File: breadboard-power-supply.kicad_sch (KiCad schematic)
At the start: 0 parts

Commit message: most of sch done
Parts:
- added C1, C4: 100nF, symbol DSE-Passives:C
- added C2, C6: 1uF, symbol DSE-Passives:C
- added C3, C5: 10uF, symbol DSE-Passives:C
- added D1, D2, D3, D4: ES1B-13-F, symbol DSE-Passives:D
- added J1, J2: PJ-002A, symbol Connector:Barrel_Jack_Switch
- added J3, J4, J5, J6: 61300211121, symbol Connector:Conn_01x02_Pin
- added R1, R4: 240R, symbol DSE-Passives:R
- added R2, R3: 390R, symbol DSE-Passives:R
- added R2, R5: 715R, symbol DSE-Passives:R
- added SW1, SW2: SW_SP3T, symbol Switch:SW_SP3T
- added SW3, SW4: 500SSP3S1M6QEA, symbol Switch:SW_SPDT
- added SW5: SW_DP3T, symbol Switch:SW_DP3T
- added U1, U2: LM317M, symbol lib_sch:LM317M
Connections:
- new net: R3.1, SW2.4
- new net: J2.1, SW4.2 (B)
- new net: R2.1, SW1.4
- new net: R2.1, SW1.2
- new net: J1.1, SW3.2 (B)
- new net: R5.1, SW2.2
- new net ADJ1: C3.1, C5.1, D2.1, D4.1, R1.2, R4.2, SW1.3, SW5.3, U1.1 (Adj), U2.1 (Adj)
- new net ADJ2: SW2.3
- new net GND: C1.2, C2.2, C3.2, C4.2, C5.2, C6.2, J1.2, J1.3, J2.2, J2.3, J3.2 (Pin_2), J5.2 (Pin_2), R2.2, R2.2, R3.2, R5.2
- new net VCC1: C2.1, D1.1, D2.2, J3.1 (Pin_1), R1.1, SW5.1, SW5.2, SW5.8, U1.2 (OUT), U1.4 (OUT)
- new net VCC2: C6.1, D3.1, D4.2, J5.1 (Pin_1), R4.1, U2.2 (OUT), U2.4 (OUT)
- new net VIN1: C1.1, D1.2, SW1.1, SW3.1 (A), SW5.7, U1.3 (IN)
- new net VIN2: C4.1, D3.2, SW2.1, SW4.1 (A), U2.3 (IN)
- no-connect marks 0 -> 9
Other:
- note added: "ADD INDICATOR LED"
- note added: "Vo=3V3"
- note added: "Vo=5V"

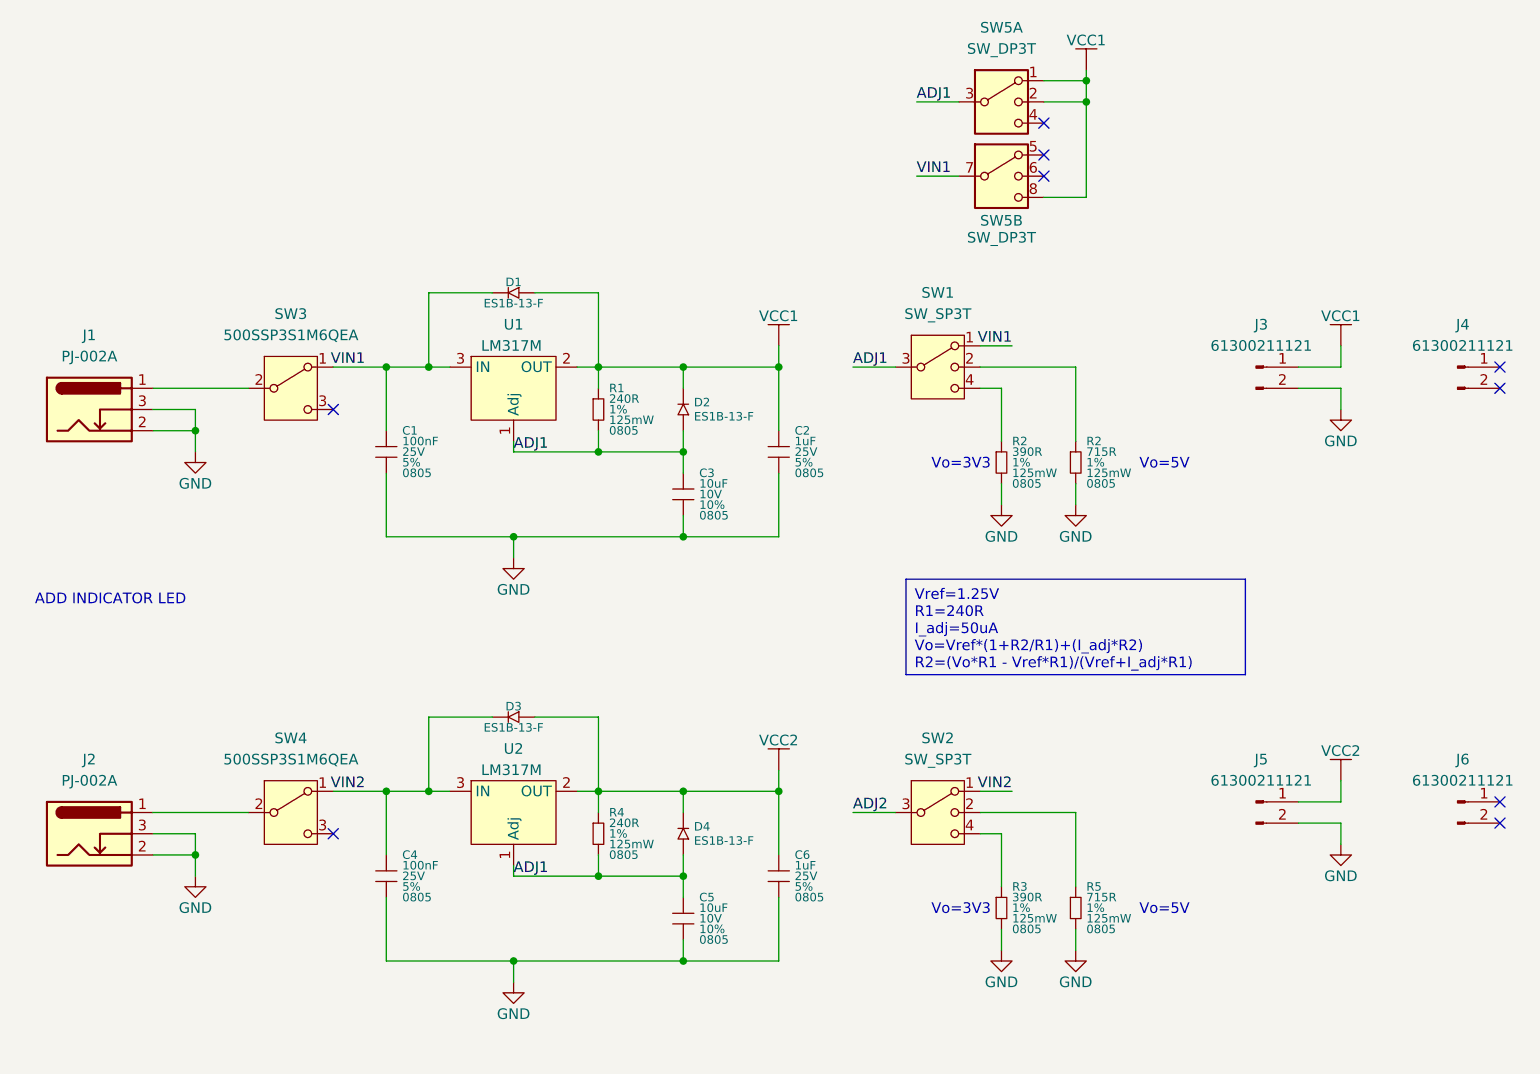
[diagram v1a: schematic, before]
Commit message: fixed switches in schematic
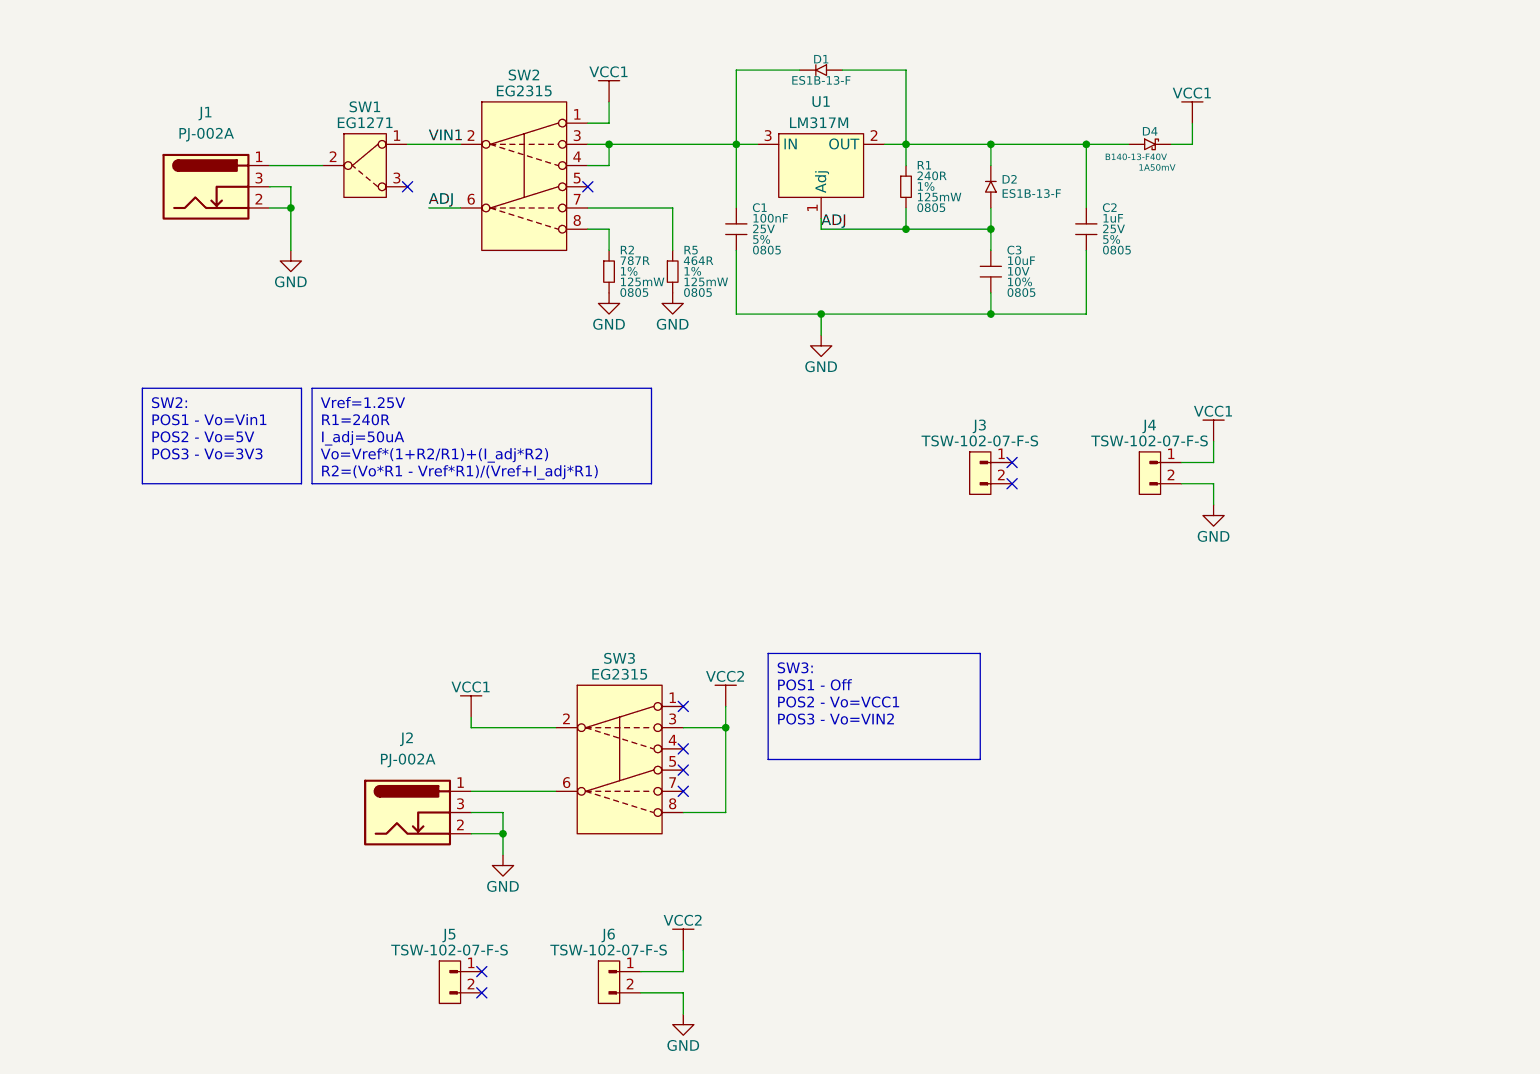
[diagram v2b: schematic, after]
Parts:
- removed C4: 100nF, symbol DSE-Passives:C
- removed C5: 10uF, symbol DSE-Passives:C
- removed C6: 1uF, symbol DSE-Passives:C
- removed D3, D4: ES1B-13-F, symbol DSE-Passives:D
- removed J2: PJ-002A, symbol Connector:Barrel_Jack_Switch
- removed J3, J4, J5, J6: 61300211121, symbol Connector:Conn_01x02_Pin
- removed R2, R3: 390R, symbol DSE-Passives:R
- removed R2, R5: 715R, symbol DSE-Passives:R
- removed R4: 240R, symbol DSE-Passives:R
- removed SW1, SW2: SW_SP3T, symbol Switch:SW_SP3T
- removed SW3, SW4: 500SSP3S1M6QEA, symbol Switch:SW_SPDT
- removed SW5: SW_DP3T, symbol Switch:SW_DP3T
- removed U2: LM317M, symbol lib_sch:LM317M
- added D4: B140-13-F, lib_fp:SMA, symbol lib_sch:D_Schottky_horizontal
- added J2: PJ-002A, lib_fp:PJ-002A, symbol lib_sch:Barrel_Jack_Switch
- added J3, J4, J5, J6: TSW-102-07-F-S, lib_fp:conn_01x02_254, symbol lib_sch:conn_01x02
- added R2: 787R, lib_fp:RESC200X125X60L35_35N, symbol lib_sch:R
- added R5: 464R, lib_fp:RESC200X125X60L35_35N, symbol lib_sch:R
- added SW1: EG1271, lib_fp:EG-1271, symbol lib_sch:EG-1271
- added SW2, SW3: EG2315, lib_fp:EG-2315, symbol lib_sch:DP3T
- C1, C2, C3: footprint (none) -> lib_fp:CAPC200X125X88L50N; symbol DSE-Passives:C -> lib_sch:C
- D1, D2: footprint (none) -> lib_fp:SMA; symbol DSE-Passives:D -> lib_sch:D
- J1: footprint (none) -> lib_fp:PJ-002A; symbol Connector:Barrel_Jack_Switch -> lib_sch:Barrel_Jack_Switch
- R1: footprint (none) -> lib_fp:RESC200X125X60L35_35N; symbol DSE-Passives:R -> lib_sch:R
- U1: footprint (none) -> lib_fp:SOT223-4
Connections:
- net GND: now also J2.2, J2.3, J4.2, J6.2, R2.2, R5.2
- net VCC1: now also D4.2, J4.1, SW2.1, SW3.2; no longer C2.1, D1.1, D2.2, R1.1, U1.2 (OUT), U1.4 (OUT)
- net VCC2: now also J6.1, SW3.3, SW3.8
- net VIN1: now also SW1.1, SW1.4, SW2.2; no longer C1.1, D1.2, U1.3 (IN)
- net at J1.1: now also SW1.2, SW1.5
- net ADJ1 renamed ADJ
- net ADJ: now also SW2.6
- new net: C2.1, D1.1, D2.2, D4.1, R1.1, U1.2 (OUT), U1.4 (OUT)
- new net: C1.1, D1.2, SW2.3, SW2.4, U1.3 (IN)
- new net: R5.1, SW2.7
- new net: R2.1, SW2.8
- new net: J2.1, SW3.6
- new net: SW1.3, SW1.6
- no-connect marks 9 -> 10
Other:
- note removed: "ADD INDICATOR LED"
- note removed: "Vo=3V3"
- note removed: "Vo=5V"
- moved on the sheet: C1, C2, C3, D1, D2, J1, R1, U1

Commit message: cleaned up files and scrubbed meta data
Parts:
- renumbered D4 to D3, R5 to R3
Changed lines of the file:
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@@
 		(dnp no)
 		(fields_autoplaced yes)
-		(property "Reference" "R5"
+		(property "Reference" "R3"
 			(at 134.62 85.09 0)
 			(do_not_autoplace yes)
@@
 			(project "breadboard-power-supply"
 				(path "/b84480f7-2a4a-488c-b5cb-7253df0ad470"
-					(reference "R5")
+					(reference "R3")
 					(unit 1)
 				)
@@
 		(dnp no)
 		(fields_autoplaced yes)
-		(property "Reference" "D4"
+		(property "Reference" "D3"
 			(at 190.5 70.866 0)
 			(do_not_autoplace yes)
@@
 			(project ""
 				(path "/b84480f7-2a4a-488c-b5cb-7253df0ad470"
-					(reference "D4")
+					(reference "D3")
 					(unit 1)
 				)
@@
 			)
 		)
-		(property "Datasheet" "datasheets/E-Switches-EG-Series"
+		(property "Datasheet" "datasheets/E-Switch-EG-Series.pdf"
 			(at 96.52 74.93 0)
 			(effects
@@
 			)
 		)
-		(property "Datasheet" "datasheets/E-Switches-EG-Series.pdf"
+		(property "Datasheet" "datasheets/E-Switch-EG-Series.pdf"
 			(at 115.57 69.85 0)
 			(effects
@@
 			)
 		)
-		(property "Datasheet" "datasheets/E-Switches-EG-Series.pdf"
+		(property "Datasheet" "datasheets/E-Switch-EG-Series.pdf"
 			(at 127 139.7 0)
 			(effects

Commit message: fixed diodes rotation and fixed voltage divider
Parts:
- R1: value 240R -> 280R; DKPN 541-240CCT-ND -> 541-280CCT-ND; MPN CRCW0805240RFKEA -> CRCW0805280RFKEA
- R2: value 787R -> 510R; DKPN 541-787CCT-ND -> 541-510CCT-ND; MPN CRCW0805787RFKEA -> CRCW0805510RFKEA
- R3: value 464R -> 887R; DKPN 541-464CCT-ND -> 541-887CCT-ND; MPN CRCW0805464RFKEA -> CRCW0805887RFKEA
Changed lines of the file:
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@@
 			)
 		)
-		(property "Value" "240R"
+		(property "Value" "280R"
 			(at 162.56 76.2 0)
 			(do_not_autoplace yes)
@@
 			)
 		)
-		(property "Description" ""
+		(property "Description" "RES SMD 280 OHM 1% 1/8W 0805"
 			(at 161.29 77.47 0)
 			(effects
@@
 			)
 		)
-		(property "MPN" "CRCW0805240RFKEA"
+		(property "MPN" "CRCW0805280RFKEA"
 			(at 161.29 74.93 0)
 			(effects
@@
 			)
 		)
-		(property "DKPN" "541-240CCT-ND"
+		(property "DKPN" "541-280CCT-ND"
 			(at 161.29 77.47 0)
 			(effects
@@
 			)
 		)
-		(property "Value" "464R"
+		(property "Value" "887R"
 			(at 134.62 86.36 0)
 			(do_not_autoplace yes)
@@
 			)
 		)
-		(property "Description" ""
+		(property "Description" "RES SMD 887 OHM 1% 1/8W 0805"
 			(at 133.35 87.63 0)
 			(effects
@@
 			)
 		)
-		(property "MPN" "CRCW0805464RFKEA"
+		(property "MPN" "CRCW0805887RFKEA"
 			(at 133.35 85.09 0)
 			(effects
@@
 			)
 		)
-		(property "DKPN" "541-464CCT-ND"
+		(property "DKPN" "541-887CCT-ND"
 			(at 133.35 87.63 0)
 			(effects
@@
 			)
 		)
-		(property "Value" "787R"
+		(property "Value" "510R"
 			(at 127 86.36 0)
 			(do_not_autoplace yes)
@@
 			)
 		)
-		(property "Description" ""
+		(property "Description" "RES SMD 510 OHM 1% 1/8W 0805"
 			(at 125.73 87.63 0)
 			(effects
@@
 			)
 		)
-		(property "MPN" "CRCW0805787RFKEA"
+		(property "MPN" "CRCW0805510RFKEA"
 			(at 125.73 85.09 0)
 			(effects
@@
 			)
 		)
-		(property "DKPN" "541-787CCT-ND"
+		(property "DKPN" "541-510CCT-ND"
 			(at 125.73 87.63 0)
 			(effects
